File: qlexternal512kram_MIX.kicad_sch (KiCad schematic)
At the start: 15 parts, among them J1 QL_SLOT_DIN41612_CARD, J2 QL_SLOT_DIN41612_CARD, U1 HM628512BLFP-7, U2 GAL16V8B-25QP, U3 LM1117-5.0

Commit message: version pre-release 1
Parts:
- removed JP1, JP2: Jumper_2_Open, Jumper:SolderJumper-2_P1.3mm_Open_Pad1.0x1.5mm, symbol Jumper:Jumper_2_Open
- removed JP3: Jumper_3_Open, Jumper:SolderJumper-3_P1.3mm_Open_Pad1.0x1.5mm, symbol Jumper:Jumper_3_Open
- added SW1: SW_DIP_x02, Button_Switch_SMD:SW_DIP_SPSTx02_Slide_KingTek_DSHP02TS_W7.62mm_P1.27mm, symbol Switch:SW_DIP_x02
- added SW2: SW_SPDT, Button_Switch_SMD:SW_SPDT_PCM12, symbol Switch:SW_SPDT
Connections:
- net BERR: now also SW2.2 (B)
- net GND: now also SW1.1, SW1.2
- net at J2.b28 (~{BERR}): now also SW2.1 (A)
- net at R3.2, U2.17 (I03): now also SW2.3 (C)
- net at R1.2, U2.7 (I7): now also SW1.4
- net at R2.2, U2.8 (I8): now also SW1.3
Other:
- note added: "NOTE SW2: 1-2 Normal Position 2-3 For use as +256Kb with my Trump Card Install the +256K after the Trump Card"
- note removed: "NOTE JP3: 1-2 Normal Position 3-4 For use as +256Kb with my Trump Card Install the +256K after the Trump Card"

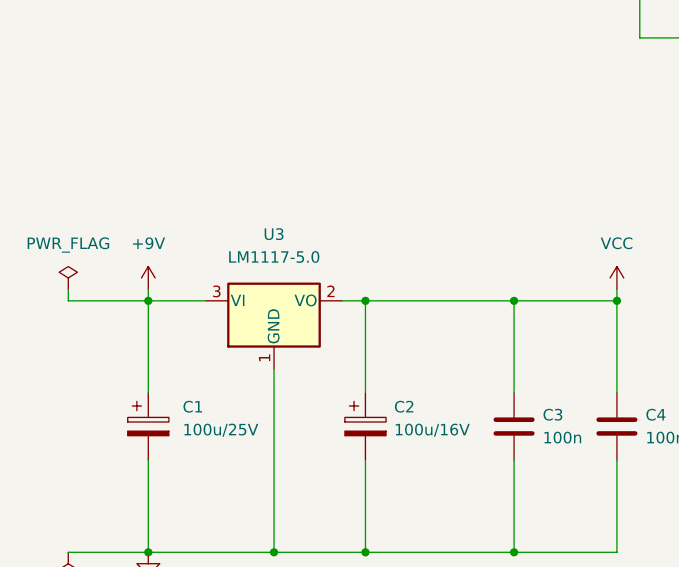
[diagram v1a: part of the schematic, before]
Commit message: updating schema and symbols
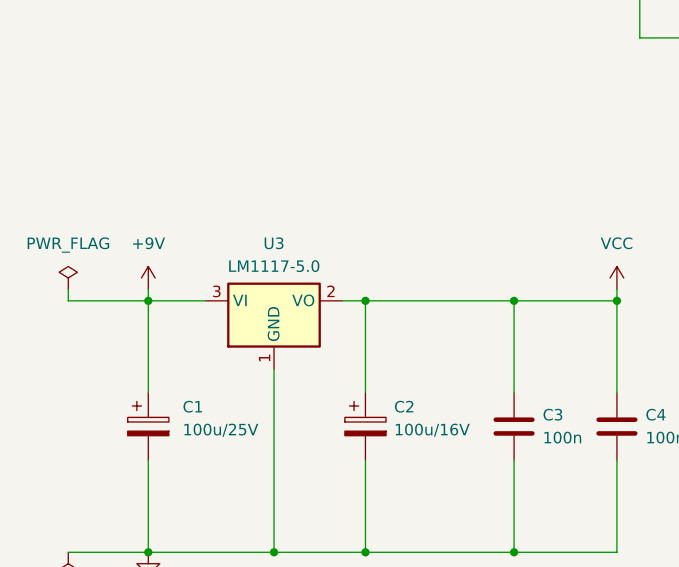
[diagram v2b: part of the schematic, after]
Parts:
- J2: footprint 8bits:DIN41612_B_2x32_Male_Horizontal_THT -> Connector_DIN:DIN41612_B_2x32_Male_Horizontal_THT
- U3: symbol Regulator_Linear:LM1117-5.0 -> Regulator_Linear:LM1117MP-5.0
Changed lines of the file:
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@@
 			)
 		)
-		(property "Description" ""
+		(property "Description" "Power symbol creates a global label with name \"GND\" , ground"
 			(at 100.33 36.83 0)
 			(effects
@@
 			)
 		)
-		(property "Description" ""
+		(property "Description" "Power symbol creates a global label with name \"+9V\""
 			(at 64.77 119.38 0)
 			(effects
@@
 			)
 		)
-		(property "Description" ""
+		(property "Description" "Power symbol creates a global label with name \"GND\" , ground"
 			(at 182.88 93.98 0)
 			(effects
@@
 			)
 		)
-		(property "Description" ""
+		(property "Description" "Power symbol creates a global label with name \"GND\" , ground"
 			(at 63.5 36.83 0)
 			(effects
@@
 			)
 		)
-		(property "Description" ""
+		(property "Description" "Power symbol creates a global label with name \"GND\" , ground"
 			(at 31.75 36.83 0)
 			(effects
@@
 	)
 	(symbol
-		(lib_id "Regulator_Linear:LM1117-5.0")
+		(lib_id "Regulator_Linear:LM1117MP-5.0")
 		(at 44.45 160.02 0)
 		(unit 1)
@@
 		(fields_autoplaced yes)
 		(property "Reference" "U3"
-			(at 44.45 152.654 0)
+			(at 44.45 153.67 0)
 			(effects
 				(font
@@
 		)
 		(property "Value" "LM1117-5.0"
-			(at 44.45 155.194 0)
+			(at 44.45 156.21 0)
 			(effects
 				(font
@@
 			)
 		)
-		(property "Description" ""
+		(property "Description" "800mA Low-Dropout Linear Regulator, 5.0V fixed output, SOT-223"
 			(at 44.45 160.02 0)
 			(effects
@@
 			)
 		)
-		(property "Description" ""
+		(property "Description" "Power symbol creates a global label with name \"GND\" , ground"
 			(at 177.8 132.08 0)
 			(effects
@@
 			)
 		)
-		(property "Footprint" "8bits:DIN41612_B_2x32_Male_Horizontal_THT"
+		(property "Footprint" "Connector_DIN:DIN41612_B_2x32_Male_Horizontal_THT"
 			(at 111.76 74.93 0)
 			(effects
@@
 			)
 		)
-		(property "Description" ""
+		(property "Description" "Power symbol creates a global label with name \"VCC\""
 			(at 82.55 158.75 0)
 			(effects
@@
 			)
 		)
-		(property "Description" ""
+		(property "Description" "Power symbol creates a global label with name \"+9V\""
 			(at 135.89 119.38 0)
 			(effects
@@
 			)
 		)
-		(property "Description" ""
+		(property "Description" "Power symbol creates a global label with name \"+9V\""
 			(at 30.48 158.75 0)
 			(effects
@@
 			)
 		)
-		(property "Description" ""
+		(property "Description" "Power symbol creates a global label with name \"VCC\""
 			(at 205.74 116.84 0)
 			(effects
@@
 			)
 		)
-		(property "Description" ""
+		(property "Description" "Power symbol creates a global label with name \"GND\" , ground"
 			(at 248.92 144.78 0)
 			(effects
@@
 			)
 		)
-		(property "Description" ""
+		(property "Description" "Power symbol creates a global label with name \"VCC\""
 			(at 248.92 106.68 0)
 			(effects
@@
 			)
 		)
-		(property "Description" ""
+		(property "Description" "Power symbol creates a global label with name \"VCC\""
 			(at 198.12 116.84 0)
 			(effects
@@
 			)
 		)
-		(property "Description" ""
+		(property "Description" "Power symbol creates a global label with name \"GND\" , ground"
 			(at 134.62 36.83 0)
 			(effects
@@
 			)
 		)
-		(property "Description" ""
+		(property "Description" "Special symbol for telling ERC where power comes from"
 			(at 21.59 158.75 0)
 			(effects
@@
 			)
 		)
-		(property "Description" ""
+		(property "Description" "Power symbol creates a global label with name \"VCC\""
 			(at 182.88 35.56 0)
 			(effects
@@
 			)
 		)
-		(property "Description" ""
+		(property "Description" "Special symbol for telling ERC where power comes from"
 			(at 21.59 187.96 0)
 			(effects
@@
 			)
 		)
-		(property "Description" ""
+		(property "Description" "Power symbol creates a global label with name \"GND\" , ground"
 			(at 30.48 187.96 0)
 			(effects
@@
 			)
 		)
-		(property "Description" ""
+		(property "Description" "Power symbol creates a global label with name \"VCC\""
 			(at 219.71 88.9 0)
 			(effects
